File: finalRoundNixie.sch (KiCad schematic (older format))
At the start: 56 parts, among them J1 Conn_01x06_Male, J2 HV_IN, J3 Conn_01x06_Female, J4 HV_OUT, Q1 MMBTA42LT1, Q10 MMBTA42LT1, Q11 AO3400, Q12 AO3400, Q13 AO3400, Q2 MMBTA42LT1, Q3 MMBTA42LT1, Q4 MMBTA42LT1, Q5 MMBTA42LT1, Q6 MMBTA42LT1, Q7 MMBTA42LT1, Q8 MMBTA42LT1, Q9 MMBTA42LT1, U1 74HC595D, U2 nixie-tube, U3 74HC595D, U4 ams1117-5.0

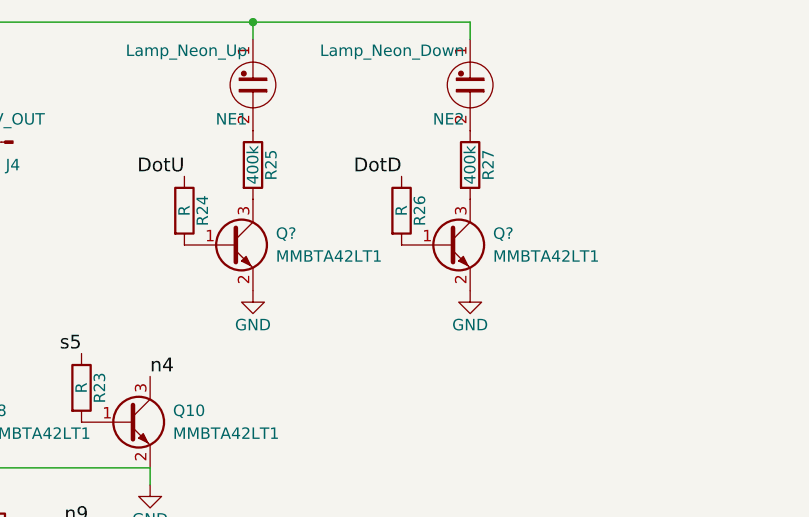
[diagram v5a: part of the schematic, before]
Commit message: fixed ams1117 pin numbering errors
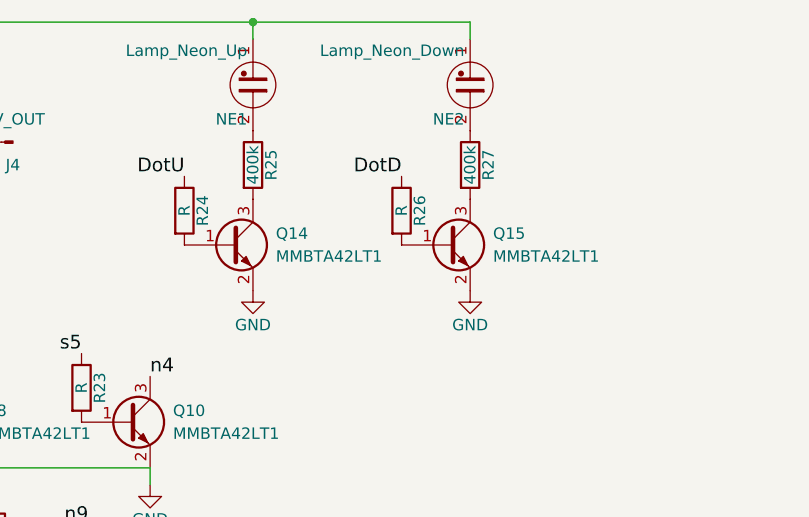
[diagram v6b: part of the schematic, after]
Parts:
- gave numbers to parts that had none: 2
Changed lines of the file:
@@
 $EndComp
 $Comp
-L Q_NPN_BEC Q?
+L Q_NPN_BEC Q14
 U 1 1 5A11319C
 P 7675 2150
-F 0 "Q?" H 7875 2200 50  0000 L CNN
+F 0 "Q14" H 7875 2200 50  0000 L CNN
 F 1 "MMBTA42LT1" H 7875 2100 50  0000 L CNN
 F 2 "TO_SOT_Packages_SMD:SOT-23" H 7875 2250 50  0001 C CNN
@@
 $EndComp
 $Comp
-L Q_NPN_BEC Q?
+L Q_NPN_BEC Q15
 U 1 1 5A113281
 P 8625 2150
-F 0 "Q?" H 8825 2200 50  0000 L CNN
+F 0 "Q15" H 8825 2200 50  0000 L CNN
 F 1 "MMBTA42LT1" H 8825 2100 50  0000 L CNN
 F 2 "TO_SOT_Packages_SMD:SOT-23" H 8825 2250 50  0001 C CNN

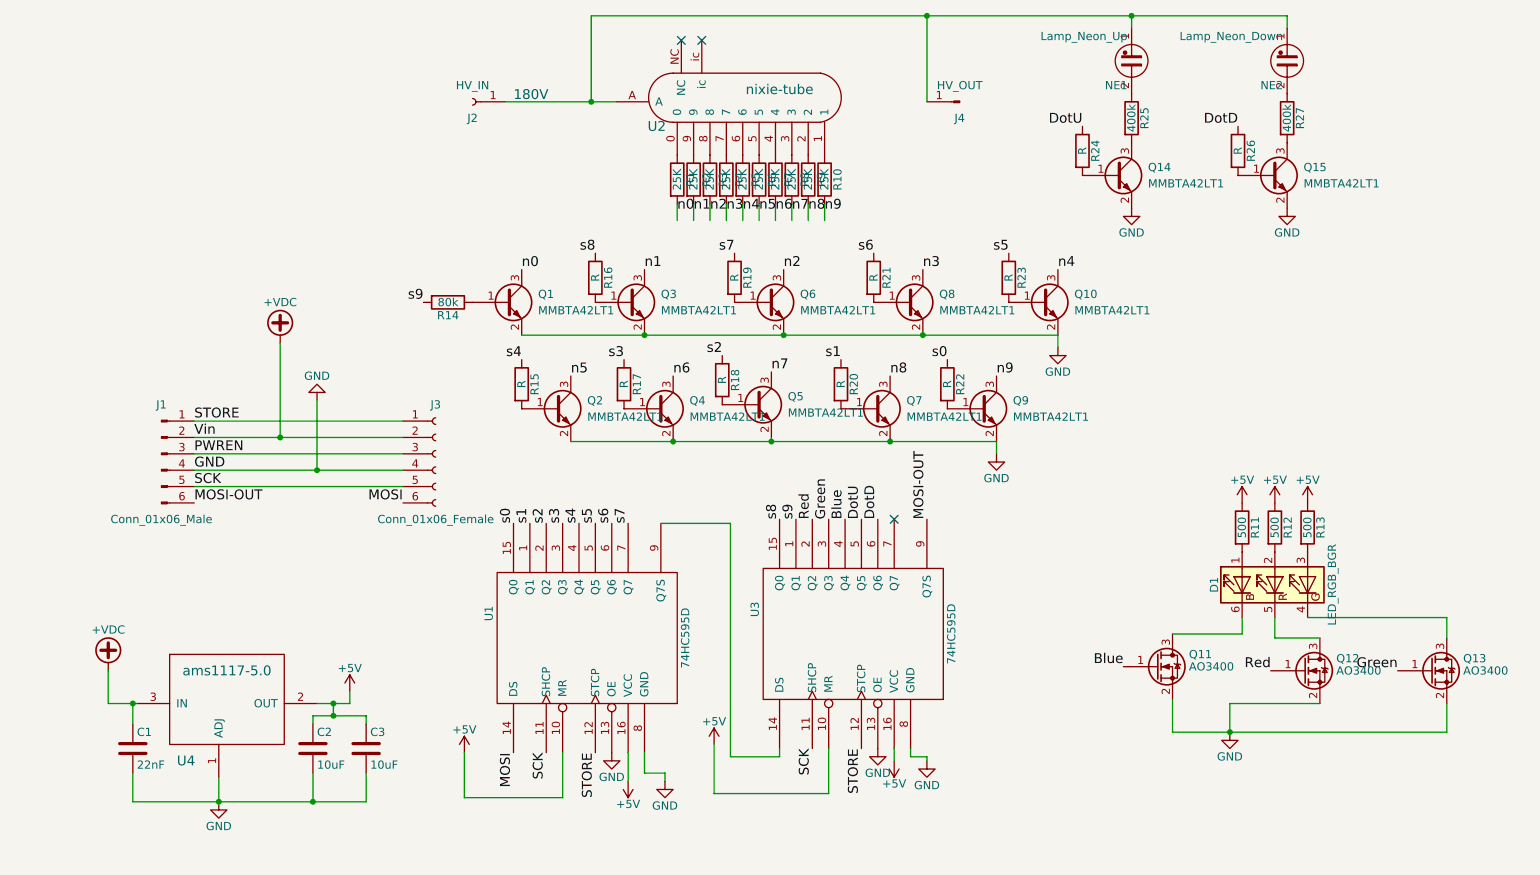
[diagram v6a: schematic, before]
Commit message: nixie's legs pin assignment needs to be change
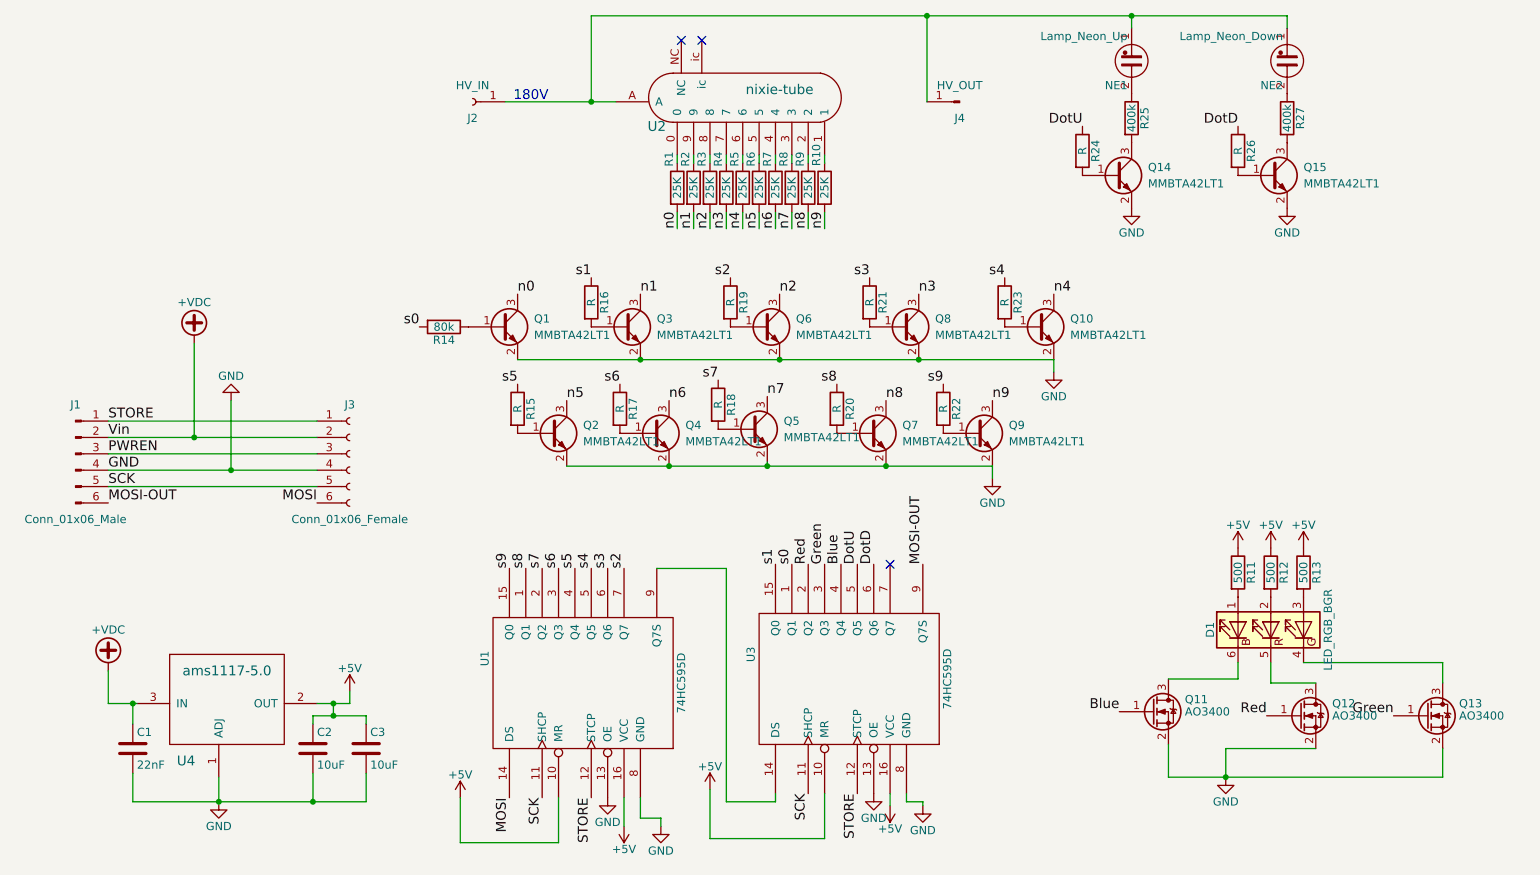
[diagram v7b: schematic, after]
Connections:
- wire segments 71 -> 81
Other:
- moved on the sheet: D1, J1, J3, Q1, Q10, Q11, Q12, Q13, Q2, Q3, Q4, Q5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
